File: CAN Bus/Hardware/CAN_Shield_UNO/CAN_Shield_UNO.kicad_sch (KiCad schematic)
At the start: 9 parts, among them J1 Power, J2 Digital/PWM, J3 Analog, J4 Digital/PWM, J6 Screw_Terminal_01x02, U2 TCAN1051HGV-Q1

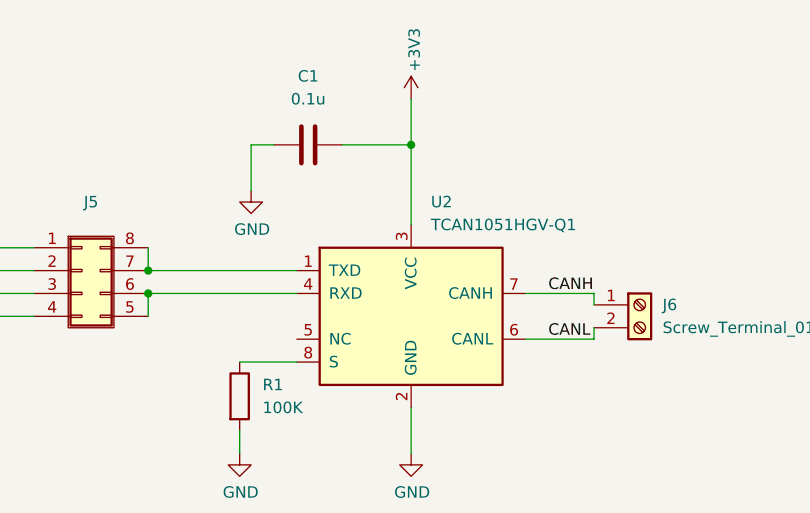
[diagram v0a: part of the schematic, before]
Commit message: fix: change the transeiver, change supply voltages
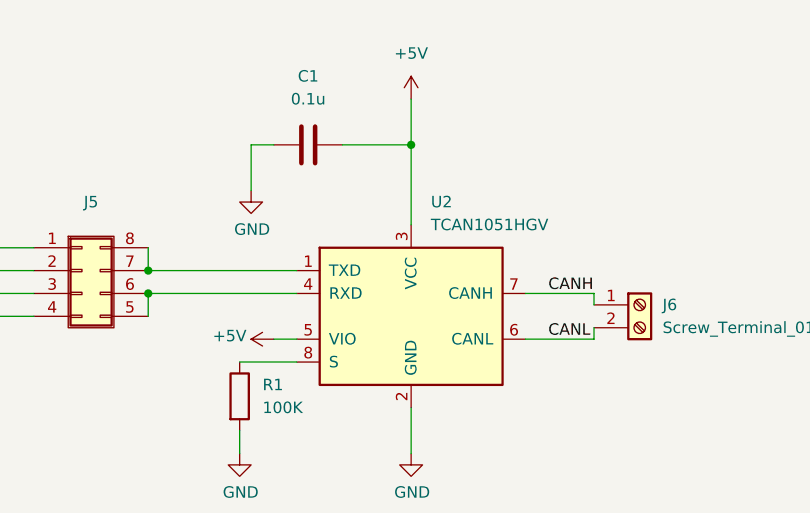
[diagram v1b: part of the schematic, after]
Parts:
- U2: value TCAN1051HGV-Q1 -> TCAN1051HGV
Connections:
- net +3V3: no longer C1.2, U2.3 (VCC)
- net +5V: now also C1.2, U2.3 (VCC), U2.5 (VIO)
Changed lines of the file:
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@@
+	(wire
+		(pts
+			(xy 128.27 53.34) (xy 130.81 53.34)
+		)
+		(stroke
+			(width 0)
+			(type default)
+		)
+	)
 	(wire
 		(pts
@@
 	)
 	(symbol
+		(lib_id "power:+5V")
+		(at 128.27 53.34 90)
+		(unit 1)
+		(exclude_from_sim no)
+		(in_bom yes)
+		(on_board yes)
+		(dnp no)
+		(property "Reference" "#PWR08"
+			(at 132.08 53.34 0)
+			(effects
+				(font
+					(size 1.27 1.27)
+				)
+				(hide yes)
+			)
+		)
+		(property "Value" "+5V"
+			(at 125.222 52.9844 90)
+			(effects
+				(font
+					(size 1.27 1.27)
+				)
+				(justify left)
+			)
+		)
+		(property "Footprint" ""
+			(at 128.27 53.34 0)
+			(effects
+				(font
+					(size 1.27 1.27)
+				)
+			)
+		)
+		(property "Datasheet" ""
+			(at 128.27 53.34 0)
+			(effects
+				(font
+					(size 1.27 1.27)
+				)
+			)
+		)
+		(property "Description" ""
+			(at 128.27 53.34 0)
+			(effects
+				(font
+					(size 1.27 1.27)
+				)
+				(hide yes)
+			)
+		)
+		(pin "1"
+		)
+		(instances
+			(project "CAN_Shield_UNO"
+				(path "/e63e39d7-6ac0-4ffd-8aa3-1841a4541b55"
+					(reference "#PWR08")
+					(unit 1)
+				)
+			)
+		)
+	)
+	(symbol
 		(lib_id "Connector:Screw_Terminal_01x02")
 		(at 168.91 49.53 0)
@@
 			)
 		)
-		(property "Value" "TCAN1051HGV-Q1"
+		(property "Value" "TCAN1051HGV"
 			(at 145.7041 40.64 0)
 			(effects
@@
 			)
 		)
-		(property "Datasheet" ""
+		(property "Datasheet" "https://www.ti.com/lit/ds/symlink/tcan1051h.pdf?ts=1712173786258&ref_url=https%253A%252F%252Fwww.ti.com%252Fsitesearch%252Fen-us%252Fdocs%252Funiversalsearch.tsp%253FlangPref%253Den-US"
 			(at 143.51 29.972 0)
 			(effects
@@
 	)
 	(symbol
+		(lib_name "+5V_1")
+		(lib_id "power:+5V")
+		(at 143.51 26.67 0)
+		(unit 1)
+		(exclude_from_sim no)
+		(in_bom yes)
+		(on_board yes)
+		(dnp no)
+		(fields_autoplaced yes)
+		(property "Reference" "#PWR010"
+			(at 143.51 30.48 0)
+			(effects
+				(font
+					(size 1.27 1.27)
+				)
+				(hide yes)
+			)
+		)
+		(property "Value" "+5V"
+			(at 143.51 21.59 0)
+			(effects
+				(font
+					(size 1.27 1.27)
+				)
+			)
+		)
+		(property "Footprint" ""
+			(at 143.51 26.67 0)
+			(effects
+				(font
+					(size 1.27 1.27)
+				)
+				(hide yes)
+			)
+		)
+		(property "Datasheet" ""
+			(at 143.51 26.67 0)
+			(effects
+				(font
+					(size 1.27 1.27)
+				)
+				(hide yes)
+			)
+		)
+		(property "Description" "Power symbol creates a global label with name \"+5V\""
+			(at 143.51 26.67 0)
+			(effects
+				(font
+					(size 1.27 1.27)
+				)
+				(hide yes)
+			)
+		)
+		(pin "1"
+		)
+		(instances
+			(project "CAN_Shield_UNO"
+				(path "/e63e39d7-6ac0-4ffd-8aa3-1841a4541b55"
+					(reference "#PWR010")
+					(unit 1)
+				)
+			)
+		)
+	)
+	(symbol
 		(lib_id "power:GND")
 		(at 143.51 66.04 0)
@@
 					(unit 1)
 				)
-			)
-		)
-	)
-	(symbol
-		(lib_id "power:+3V3")
-		(at 143.51 26.67 0)
-		(unit 1)
-		(exclude_from_sim no)
-		(in_bom yes)
-		(on_board yes)
-		(dnp no)
-		(property "Reference" "#PWR08"
-			(at 143.51 30.48 0)
-			(effects
-				(font
-					(size 1.27 1.27)
-				)
-				(hide yes)
-			)
-		)
-		(property "Value" "+3V3"
-			(at 143.891 23.622 90)
-			(effects
-				(font
-					(size 1.27 1.27)
-				)
-				(justify left)
-			)
-		)
-		(property "Footprint" ""
-			(at 143.51 26.67 0)
-			(effects
-				(font
-					(size 1.27 1.27)
-				)
-			)
-		)
-		(property "Datasheet" ""
-			(at 143.51 26.67 0)
-			(effects
-				(font
-					(size 1.27 1.27)
-				)
-			)
-		)
-		(property "Description" ""
-			(at 143.51 26.67 0)
-			(effects
-				(font
-					(size 1.27 1.27)
-				)
-				(hide yes)
-			)
-		)
-		(pin "1"
-		)
-		(instances
-			(project "CAN_Shield_UNO"
-				(path "/e63e39d7-6ac0-4ffd-8aa3-1841a4541b55"
-					(reference "#PWR08")
-					(unit 1)
-				)
